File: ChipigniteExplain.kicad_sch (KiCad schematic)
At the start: 73 parts, among them J1 Conn_01x02, J2 Conn_01x02, J3 Conn_01x03, J4 USB_C, J5 613012243121, J6 613012243121, J7 Conn_02x03_Odd_Even, Q1 DMN2005K, SW1 434121025816, SW2 434121025816, SW6 193-8MSR, U1 TLV1117LV33, U2 TPD1E05U06QDPYRQ1, U3 157112V12700

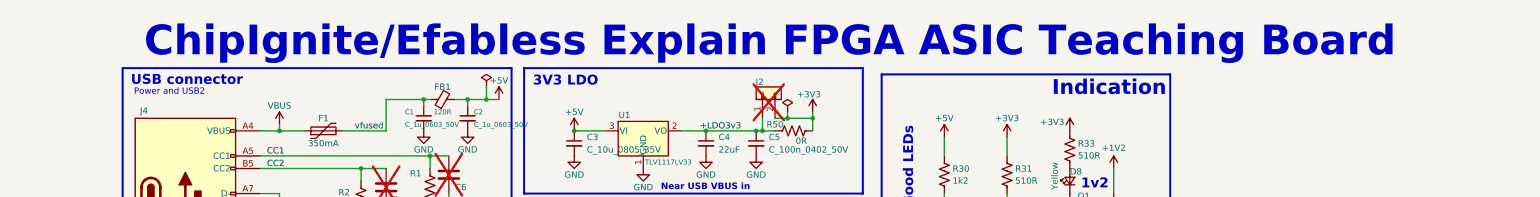
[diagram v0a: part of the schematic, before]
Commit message: revised to remove EF branding, adjust LED resistors, and invert SW2 button for reset.
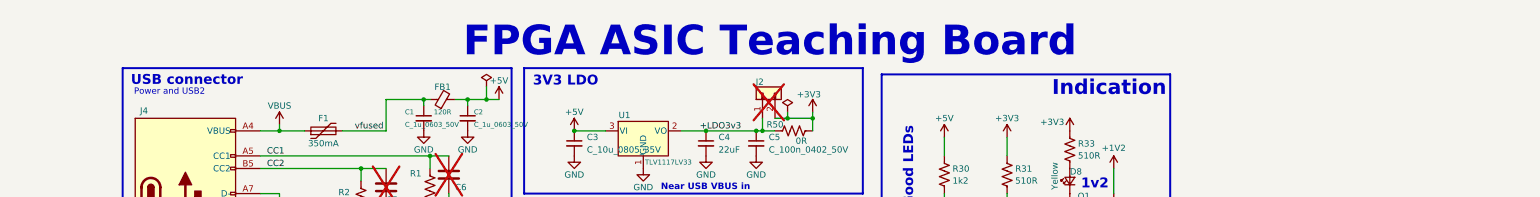
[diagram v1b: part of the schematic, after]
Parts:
- R42, R43, R44, R45, R46, R47, R48, R49: value 510R -> 68R
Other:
- note added: "FPGA ASIC Teaching Board"
- note removed: "ChipIgnite/Efabless Explain FPGA ASIC Teaching Board"
